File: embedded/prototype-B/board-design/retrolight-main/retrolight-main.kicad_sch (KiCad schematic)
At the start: 32 parts, among them J1 Conn_02x05_Odd_Even, U1 TLC59108xPW

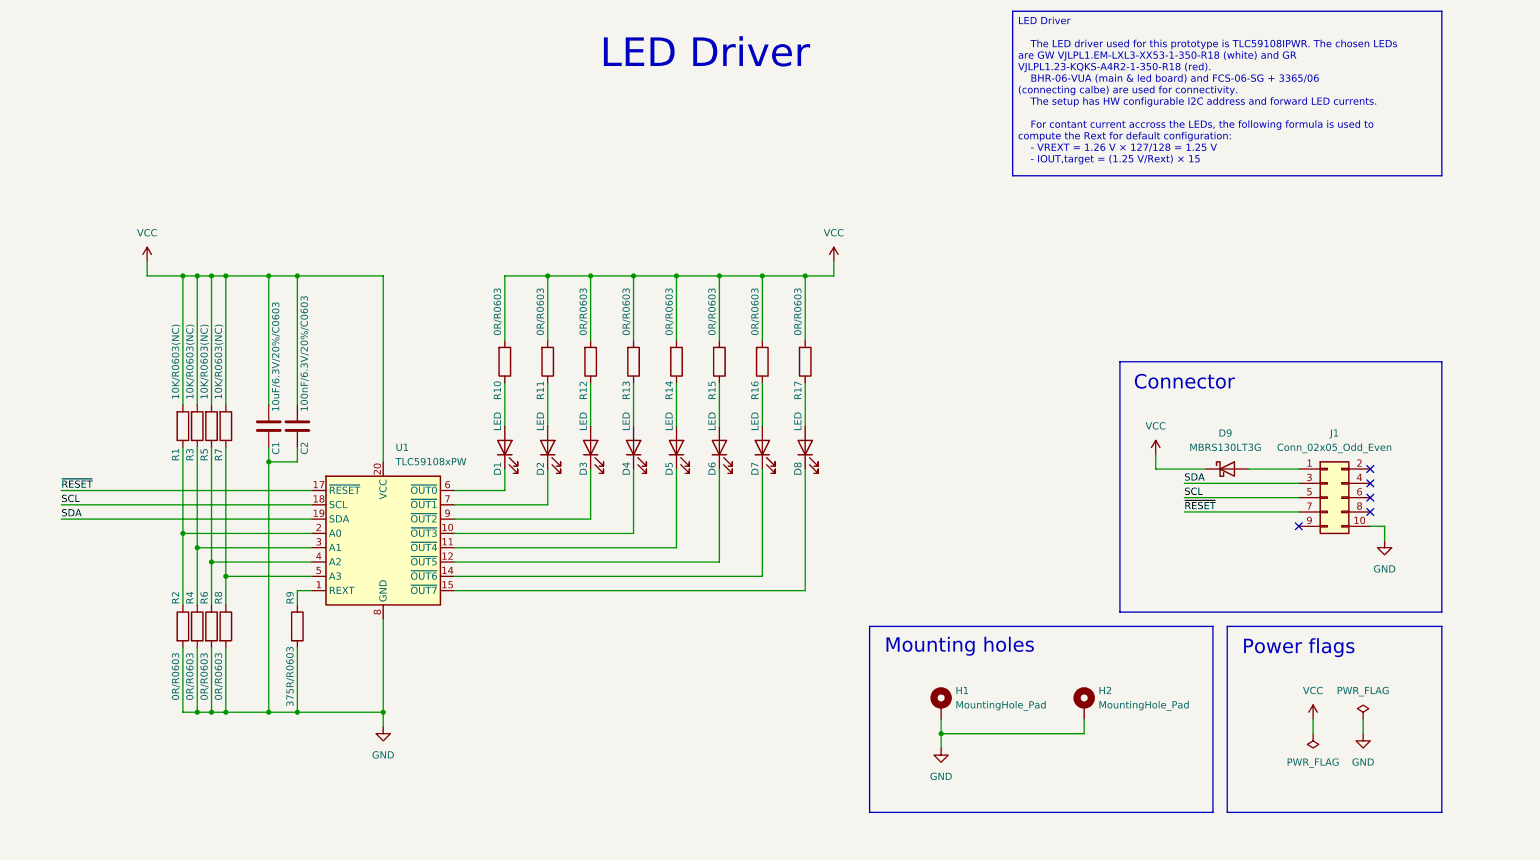
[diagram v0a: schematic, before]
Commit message: [Light] Led driver reset pin enhacement
Refactored lighting PCB.

Signed-off-by: Nicolae-Andrei Prodan <vasilenicolaeandrei@gmail.com>
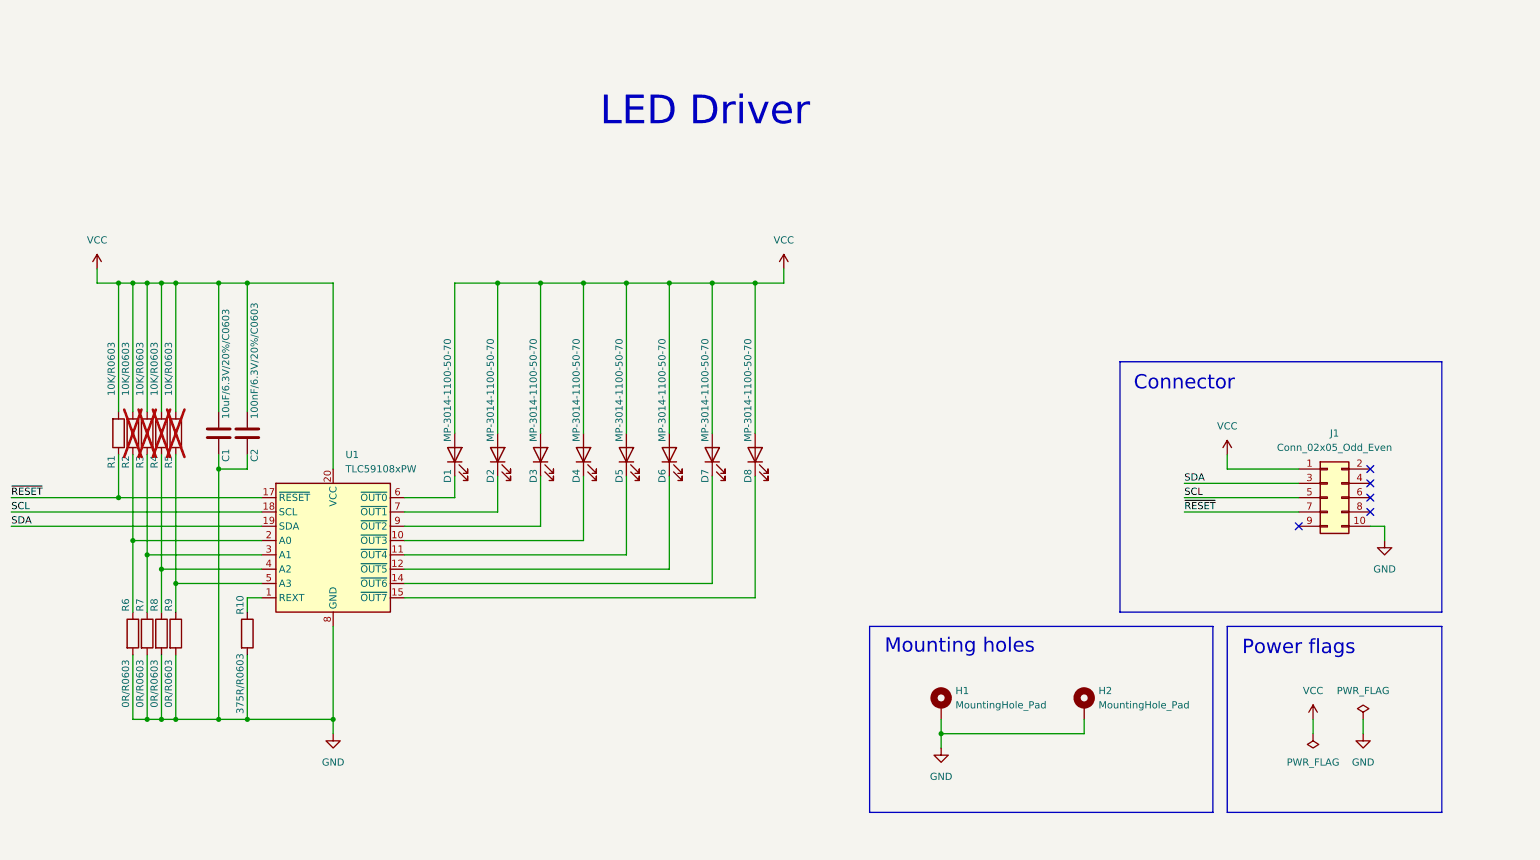
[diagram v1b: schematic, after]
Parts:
- removed D9: MBRS130LT3G, Diode_SMD:D_SMB, symbol Device:D_Schottky
- removed R10, R11, R12, R13, R14, R15, R16, R17: 0R/R0603, Resistor_SMD:R_0603_1608Metric_Pad0.98x0.95mm_HandSolder, symbol Device:R
- added R1: 10K/R0603, Resistor_SMD:R_0603_1608Metric_Pad0.98x0.95mm_HandSolder, symbol Device:R
- D1, D2, D3, D4, D5, D6, D7, D8: value LED -> MP-3014-1100-50-70; footprint LED:LED_0505_1313Metric -> LED_SMD:LED_1206_3216Metric_Pad1.42x1.75mm_HandSolder
- R2: renamed from R1; value 10K/R0603(NC) -> 10K/R0603; now not fitted
- R3: value 10K/R0603(NC) -> 10K/R0603; now not fitted
- R4: renamed from R5; value 10K/R0603(NC) -> 10K/R0603; now not fitted
- R5: renamed from R7; value 10K/R0603(NC) -> 10K/R0603; now not fitted
- renumbered R9 to R10, R2 to R6, R4 to R7, R6 to R8, R8 to R9
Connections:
- net VCC: now also D1.2 (A), D2.2 (A), D3.2 (A), D4.2 (A), D5.2 (A), D6.2 (A), D7.2 (A), D8.2 (A), J1.1 (Pin_1), R1.2
- net ~{RESET}: now also R1.1
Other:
- moved on the sheet: C1, C2, D1, R10, R6, R7, R8, R9, U1

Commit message: [Central unit] Redesign the power lines
Fixed lighting board footprint and resistor value issues. Redesigned
power path.

Signed-off-by: Nicolae-Andrei Prodan <vasilenicolaeandrei@gmail.com>
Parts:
- removed D1, D2, D3, D4, D5, D6, D7, D8: MP-3014-1100-50-70, LED_SMD:LED_1206_3216Metric_Pad1.42x1.75mm_HandSolder, symbol Device:LED
- added D1, D2, D3, D4, D5, D6, D7, D8: MP-3014-1100-50-70, MP_3014_1100_50_70:LED_MP-3014-1100-50-70, symbol MP-3014-1100-50-70:MP-3014-1100-50-70
- R10: value 375R/R0603 -> 750R/R0603
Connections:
- net VCC: now also D1.A, D2.A, D3.A, D4.A, D5.A, D6.A, D7.A, D8.A
- net at U1.11 (~{OUT4}): now also D5.C
- net at U1.12 (~{OUT5}): now also D6.C
- net at U1.10 (~{OUT3}): now also D4.C
- net at U1.14 (~{OUT6}): now also D7.C
- net at U1.15 (~{OUT7}): now also D8.C
- net at U1.6 (~{OUT0}): now also D1.C
- net at U1.7 (~{OUT1}): now also D2.C
- net at U1.9 (~{OUT2}): now also D3.C

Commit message: [All] Enhance BOM
Enhanced lighting board BOM to include PCBWay required fields

Signed-off-by: Nicolae-Andrei Prodan <vasilenicolaeandrei@gmail.com>
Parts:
- C1: value 10uF/6.3V/20%/C0603 -> 10uF/16V/10%C0603; PROD_ID (none) -> CC0603KRX5R7BB106
- C2: value 100nF/6.3V/20%/C0603 -> 100nF/16V/10%C0603; PROD_ID (none) -> CC0603KRX7R7BB104
- D1, D2, D3, D4, D5, D6, D7, D8: PROD_ID (none) -> MP-3014-1100-50-70
- J1: PROD_ID (none) -> SBH11-PBPC-D05-ST-BK
- R1, R2, R3, R4, R5: value 10K/R0603 -> 10K/0.1W/1%/R0603; PROD_ID (none) -> RC0603FR-0710KL
- R10: value 750R/R0603 -> 750R/0.1W/1%/R0603; PROD_ID (none) -> RC0603FR-07750RL
- R6, R7, R8, R9: value 0R/R0603 -> 0R/0.1W/JUMPER/R0603; PROD_ID (none) -> RC0603JR-070RL
- U1: PROD_ID (none) -> TLC59108IPWR

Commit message: [All] Enhance BOM
Refacored lighting board BOM.

Signed-off-by: Nicolae-Andrei Prodan <vasilenicolaeandrei@gmail.com>
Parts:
- C1: MPN (none) -> CC0603KRX5R7BB106; PROD_ID CC0603KRX5R7BB106 -> (none); Package (none) -> 0603 (1608 Metric)
- C2: MPN (none) -> CC0603KRX7R7BB104; PROD_ID CC0603KRX7R7BB104 -> (none); Package (none) -> 0603 (1608 Metric)
- D1, D2, D3, D4, D5, D6, D7, D8: MPN (none) -> MP-3014-1100-50-70; PROD_ID MP-3014-1100-50-70 -> (none); Package (none) -> MP-3014-1100-50-70
- J1: MPN (none) -> SBH11-PBPC-D05-ST-BK; PROD_ID SBH11-PBPC-D05-ST-BK -> (none); Package (none) -> IDC-Header_2x05_P2.54mm_Vertical
- R1, R2, R3, R4, R5: MPN (none) -> RC0603FR-0710KL; PROD_ID RC0603FR-0710KL -> (none); Package (none) -> 0603 (1608 Metric)
- R10: MPN (none) -> RC0603FR-07750RL; PROD_ID RC0603FR-07750RL -> (none); Package (none) -> 0603 (1608 Metric)
- R6, R7, R8, R9: MPN (none) -> RC0603JR-070RL; PROD_ID RC0603JR-070RL -> (none); Package (none) -> 0603 (1608 Metric)
- U1: MPN (none) -> TLC59108IPWR; PROD_ID TLC59108IPWR -> (none); Package (none) -> 20-TSSOP
